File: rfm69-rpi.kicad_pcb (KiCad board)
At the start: 2 copper layers, 65 x 56 mm, 21 parts, among them IC1 RFM69, IC2 RFM69, IC3 RFM69, IC4 RFM69, IC5 NCP1117, IC6 74HC139, J1 RPi_GPIO, P1 COAX, P2 COAX, P3 COAX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

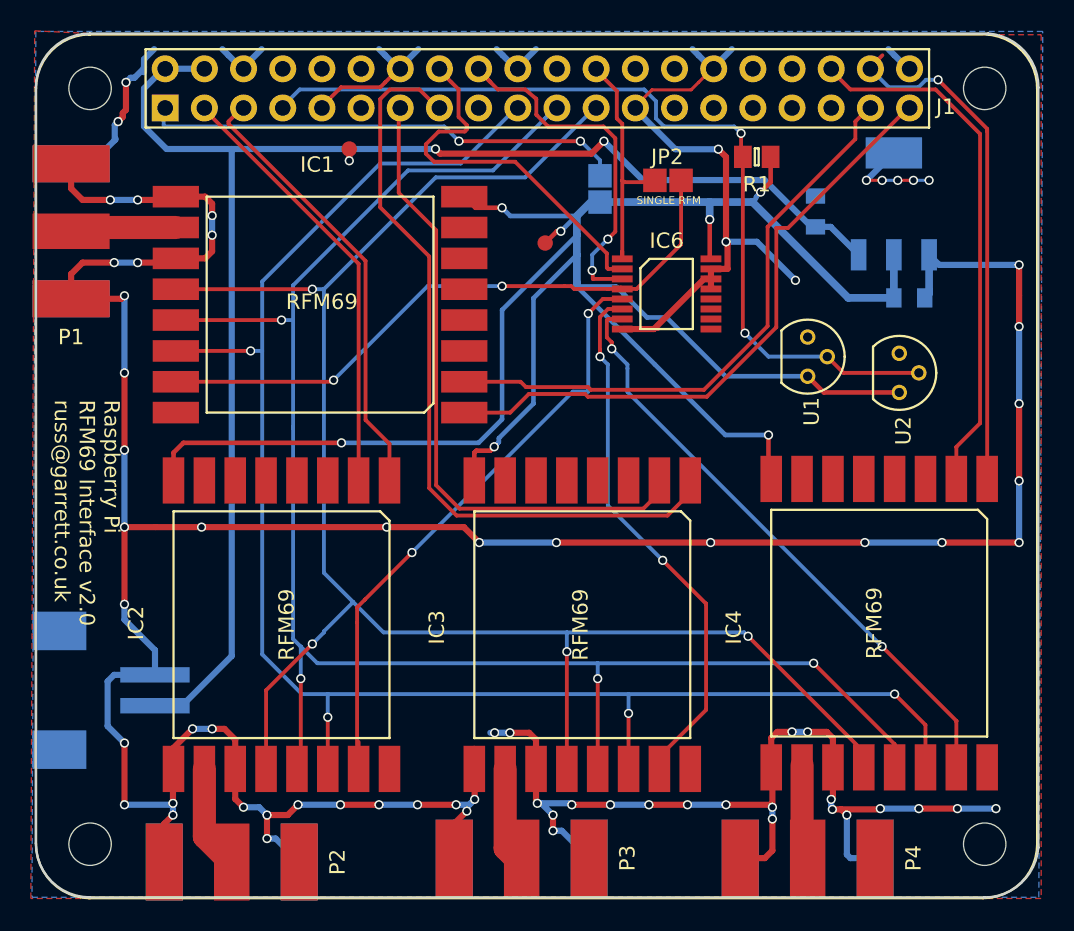
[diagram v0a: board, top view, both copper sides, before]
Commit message: Finally fixed footprint.
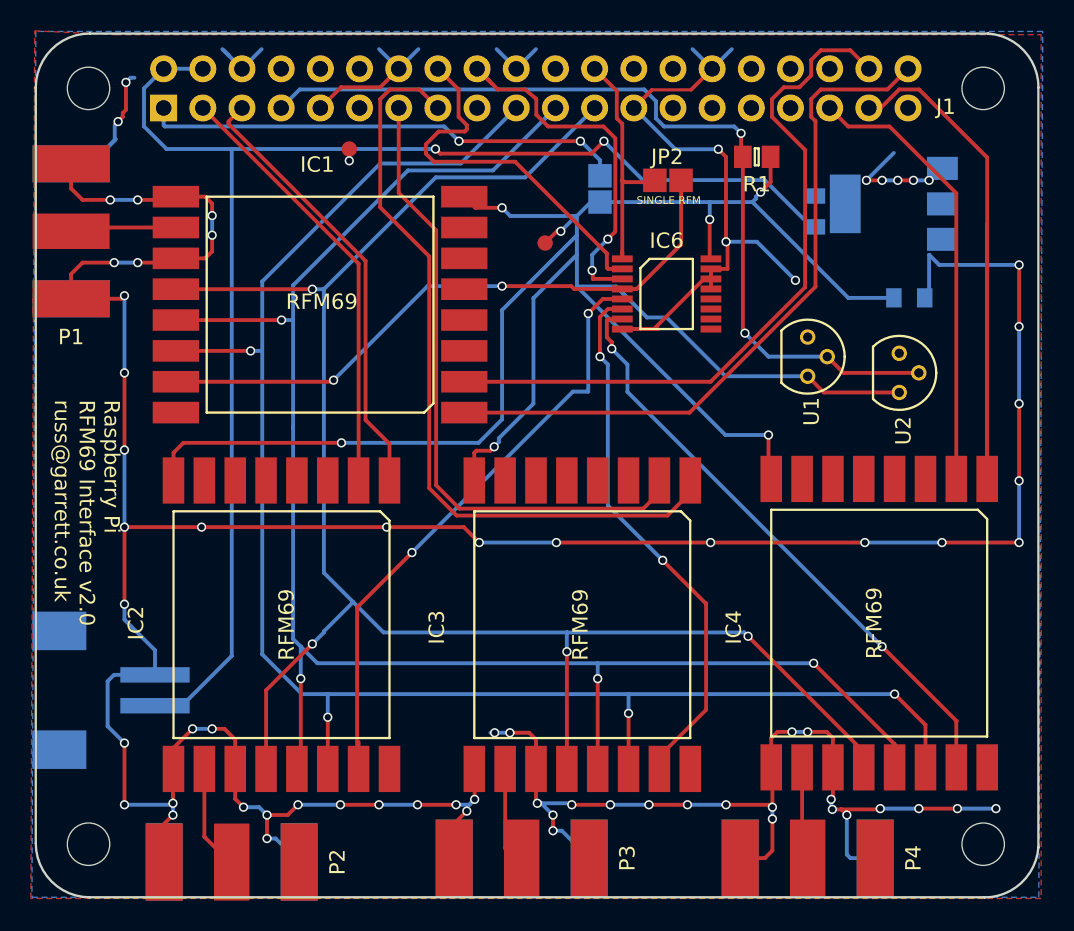
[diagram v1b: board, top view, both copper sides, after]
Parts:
- IC5: footprint SOT-223 -> Package_TO_SOT_SMD:SOT-223
- J1: footprint russ:raspberrypi2 -> pcb-rfm-raspi:raspberrypi2
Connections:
- IC1 pad 16: Net-(IC1-Pad16) -> (no net)
- IC1 pad 3: Net-(IC1-Pad3) -> (no net)
- IC1 pad 4: Net-(IC1-Pad4) -> (no net)
- IC1 pad 5: Net-(IC1-Pad5) -> (no net)
- IC1 pad 6: Net-(IC1-Pad6) -> (no net)
- IC1 pad 7: Net-(IC1-Pad7) -> (no net)
- IC2 pad 16: Net-(IC2-Pad16) -> (no net)
- IC2 pad 3: Net-(IC2-Pad3) -> (no net)
- IC2 pad 4: Net-(IC2-Pad4) -> (no net)
- IC2 pad 5: Net-(IC2-Pad5) -> (no net)
- IC2 pad 6: Net-(IC2-Pad6) -> (no net)
- IC2 pad 7: Net-(IC2-Pad7) -> (no net)
- IC3 pad 16: Net-(IC3-Pad16) -> (no net)
- IC3 pad 3: Net-(IC3-Pad3) -> (no net)
- IC3 pad 4: Net-(IC3-Pad4) -> (no net)
- IC3 pad 5: Net-(IC3-Pad5) -> (no net)
- IC3 pad 6: Net-(IC3-Pad6) -> (no net)
- IC3 pad 7: Net-(IC3-Pad7) -> (no net)
- IC4 pad 16: Net-(IC4-Pad16) -> (no net)
- IC4 pad 3: Net-(IC4-Pad3) -> (no net)
- IC4 pad 4: Net-(IC4-Pad4) -> (no net)
- IC4 pad 5: Net-(IC4-Pad5) -> (no net)
- IC4 pad 6: Net-(IC4-Pad6) -> (no net)
- IC4 pad 7: Net-(IC4-Pad7) -> (no net)
- IC5 pad 4: Earth -> (no net)
- IC6 pad 10: Net-(IC6-Pad10) -> (no net)
- IC6 pad 11: Net-(IC6-Pad11) -> (no net)
- IC6 pad 12: Net-(IC6-Pad12) -> (no net)
- IC6 pad 9: Net-(IC6-Pad9) -> (no net)
- J1 pad 10: Net-(J1-Pad10) -> (no net)
- J1 pad 11: Net-(J1-Pad11) -> (no net)
- J1 pad 12: Net-(J1-Pad12) -> (no net)
- J1 pad 17: Net-(J1-Pad17) -> (no net)
- J1 pad 22: Net-(J1-Pad22) -> (no net)
- J1 pad 26: Net-(J1-Pad26) -> (no net)
- J1 pad 27: Net-(J1-Pad27) -> (no net)
- J1 pad 28: Net-(J1-Pad28) -> (no net)
- J1 pad 29: Net-(J1-Pad29) -> (no net)
- J1 pad 31: Net-(J1-Pad31) -> (no net)
- J1 pad 32: Net-(J1-Pad32) -> (no net)
- J1 pad 33: Net-(J1-Pad33) -> (no net)
- J1 pad 36: Net-(J1-Pad36) -> (no net)
- J1 pad 8: Net-(J1-Pad8) -> (no net)
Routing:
- net RESET4: track 33.5 -> 47.4 mm, vias 1 -> 0
- net INT1: track 38.5 -> 46.4 mm
- net INT4: track 34.5 -> 29.0 mm
- net RESET1: track 40.9 -> 45.5 mm
- net Earth: track 344.8 -> 340.2 mm
- net +5V: track 98.1 -> 94.5 mm
- net +3V3: track 150.4 -> 147.6 mm
